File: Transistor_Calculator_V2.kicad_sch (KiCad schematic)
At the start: 50 parts, among them Q1 2N3904, Q10 2N3904, Q11 2N3904, Q12 2N3904, Q13 2N3904, Q14 2N3904, Q15 2N3904, Q16 2N3904, Q17 2N3904, Q18 2N3904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

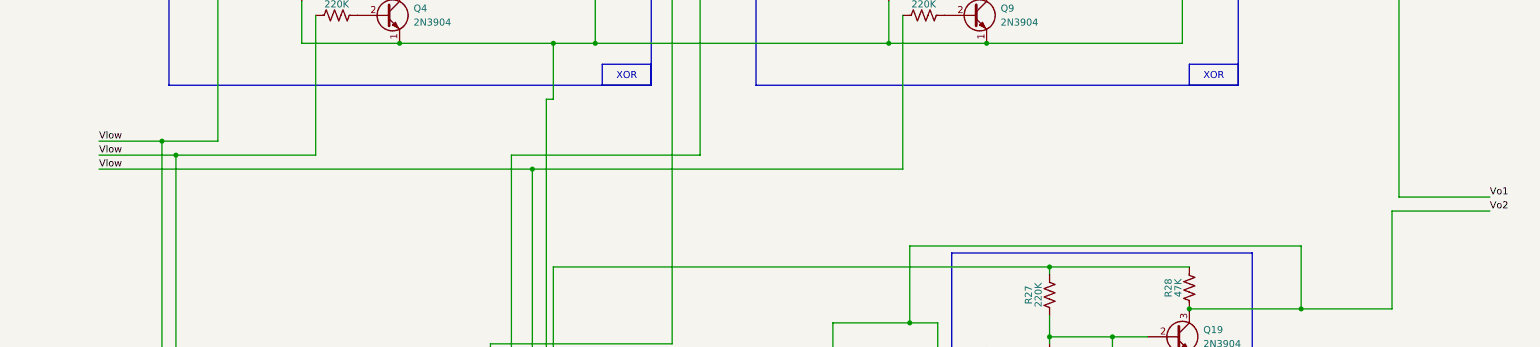
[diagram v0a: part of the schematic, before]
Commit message: added output labels
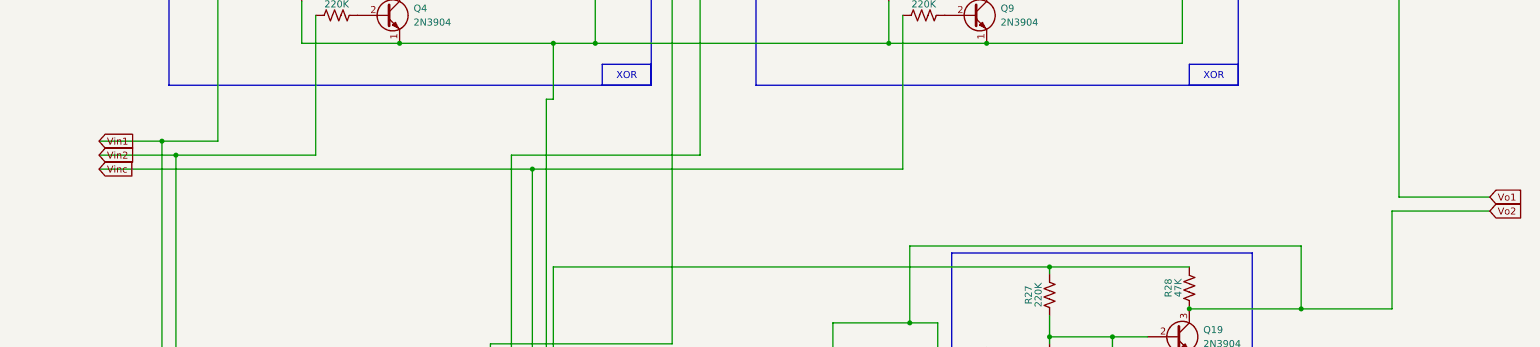
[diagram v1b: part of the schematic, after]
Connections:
- net Vlow: no longer R1.1, R10.1, R18.1, R19.1, R2.1, R21.1
- new net Vin1: R1.1, R18.1
- new net Vin2: R19.1, R2.1
- new net Vinc: R10.1, R21.1
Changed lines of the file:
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@@
-	)
-	(label "Vlow"
-		(at 17.78 105.41 0)
-		(fields_autoplaced yes)
-		(effects
-			(font
-				(size 1.27 1.27)
-			)
-			(justify left bottom)
-		)
-	)
-	(label "Vo1"
-		(at 270.51 113.03 0)
-		(fields_autoplaced yes)
-		(effects
-			(font
-				(size 1.27 1.27)
-			)
-			(justify left bottom)
-		)
 	)
 	(label "Vlow"
@@
 	(label "Vhigh"
 		(at -15.24 115.57 0)
-		(fields_autoplaced yes)
-		(effects
-			(font
-				(size 1.27 1.27)
-			)
-			(justify left bottom)
-		)
-	)
-	(label "Vlow"
-		(at 17.78 107.95 0)
-		(fields_autoplaced yes)
-		(effects
-			(font
-				(size 1.27 1.27)
-			)
-			(justify left bottom)
-		)
-	)
-	(label "Vo2"
-		(at 270.51 115.57 0)
-		(fields_autoplaced yes)
-		(effects
-			(font
-				(size 1.27 1.27)
-			)
-			(justify left bottom)
-		)
-	)
-	(label "Vlow"
-		(at 17.78 102.87 0)
 		(fields_autoplaced yes)
 		(effects
@@
 		)
 	)
+	(global_label "Vin1"
+		(shape input)
+		(at 17.78 102.87 0)
+		(fields_autoplaced yes)
+		(effects
+			(font
+				(size 1.27 1.27)
+			)
+			(justify left)
+		)
+		(property "Intersheetrefs" "${INTERSHEET_REFS}"
+			(at 24.8171 102.87 0)
+			(effects
+				(font
+					(size 1.27 1.27)
+				)
+				(justify left)
+				(hide yes)
+			)
+		)
+	)
+	(global_label "Vo1"
+		(shape input)
+		(at 270.51 113.03 0)
+		(fields_autoplaced yes)
+		(effects
+			(font
+				(size 1.27 1.27)
+			)
+			(justify left)
+		)
+		(property "Intersheetrefs" "${INTERSHEET_REFS}"
+			(at 276.9423 113.03 0)
+			(effects
+				(font
+					(size 1.27 1.27)
+				)
+				(justify left)
+				(hide yes)
+			)
+		)
+	)
+	(global_label "Vinc"
+		(shape input)
+		(at 17.78 107.95 0)
+		(fields_autoplaced yes)
+		(effects
+			(font
+				(size 1.27 1.27)
+			)
+			(justify left)
+		)
+		(property "Intersheetrefs" "${INTERSHEET_REFS}"
+			(at 24.6962 107.95 0)
+			(effects
+				(font
+					(size 1.27 1.27)
+				)
+				(justify left)
+				(hide yes)
+			)
+		)
+	)
+	(global_label "Vin2"
+		(shape input)
+		(at 17.78 105.41 0)
+		(fields_autoplaced yes)
+		(effects
+			(font
+				(size 1.27 1.27)
+			)
+			(justify left)
+		)
+		(property "Intersheetrefs" "${INTERSHEET_REFS}"
+			(at 24.8171 105.41 0)
+			(effects
+				(font
+					(size 1.27 1.27)
+				)
+				(justify left)
+				(hide yes)
+			)
+		)
+	)
+	(global_label "Vo2"
+		(shape input)
+		(at 270.51 115.57 0)
+		(fields_autoplaced yes)
+		(effects
+			(font
+				(size 1.27 1.27)
+			)
+			(justify left)
+		)
+		(property "Intersheetrefs" "${INTERSHEET_REFS}"
+			(at 276.9423 115.57 0)
+			(effects
+				(font
+					(size 1.27 1.27)
+				)
+				(justify left)
+				(hide yes)
+			)
+		)
+	)

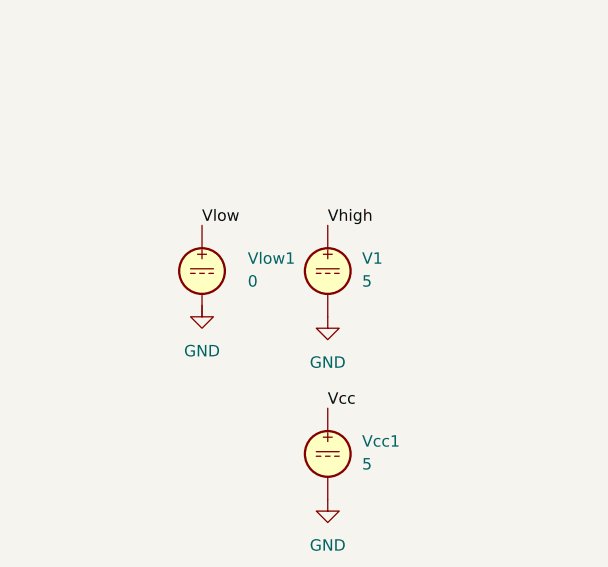
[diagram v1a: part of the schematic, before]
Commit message: Changed control of the input
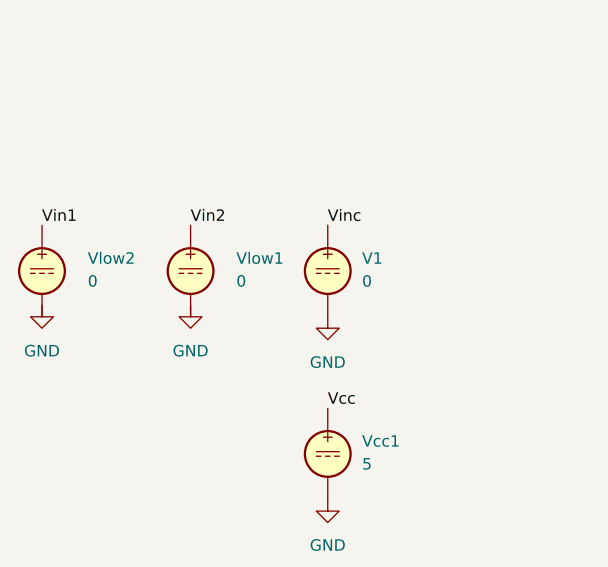
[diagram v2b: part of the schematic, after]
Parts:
- added Vlow2: 0, symbol Simulation_SPICE:VDC
- V1: value 5 -> 0
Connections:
- net Vhigh is gone; now on net Vinc: V1.1
- net Vlow is gone; now on net Vin2: Vlow1.1
- net Vin1: now also Vlow2.1
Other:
- moved on the sheet: Vlow1
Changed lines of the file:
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@@
 		)
 	)
-	(label "Vlow"
-		(at -29.21 115.57 0)
+	(label "Vin2"
+		(at -30.48 115.57 0)
 		(fields_autoplaced yes)
 		(effects
@@
 		)
 	)
-	(label "Vhigh"
+	(label "Vin1"
+		(at -46.99 115.57 0)
+		(fields_autoplaced yes)
+		(effects
+			(font
+				(size 1.27 1.27)
+			)
+			(justify left bottom)
+		)
+	)
+	(label "Vinc"
 		(at -15.24 115.57 0)
 		(fields_autoplaced yes)
@@
 	(symbol
 		(lib_id "power:GND")
-		(at -29.21 124.46 0)
+		(at -30.48 124.46 0)
 		(unit 1)
 		(exclude_from_sim no)
@@
 		(fields_autoplaced yes)
 		(property "Reference" "#PWR01"
-			(at -29.21 130.81 0)
+			(at -30.48 130.81 0)
 			(effects
 				(font
@@
 		)
 		(property "Value" "GND"
-			(at -29.21 129.54 0)
+			(at -30.48 129.54 0)
 			(effects
 				(font
@@
 		)
 		(property "Footprint" ""
-			(at -29.21 124.46 0)
+			(at -30.48 124.46 0)
 			(effects
 				(font
@@
 		)
 		(property "Datasheet" ""
-			(at -29.21 124.46 0)
+			(at -30.48 124.46 0)
 			(effects
 				(font
@@
 		)
 		(property "Description" "Power symbol creates a global label with name \"GND\" , ground"
-			(at -29.21 124.46 0)
+			(at -30.48 124.46 0)
 			(effects
 				(font
@@
 			)
 		)
-		(property "Value" "5"
+		(property "Value" "0"
 			(at -11.43 121.7901 0)
 			(effects
@@
 	(symbol
 		(lib_id "Simulation_SPICE:VDC")
-		(at -29.21 120.65 0)
+		(at -30.48 120.65 0)
 		(unit 1)
 		(exclude_from_sim no)
@@
 		(fields_autoplaced yes)
 		(property "Reference" "Vlow1"
-			(at -24.13 119.2501 0)
+			(at -25.4 119.2501 0)
 			(effects
 				(font
@@
 		)
 		(property "Value" "0"
-			(at -24.13 121.7901 0)
+			(at -25.4 121.7901 0)
 			(effects
 				(font
@@
 		)
 		(property "Footprint" ""
-			(at -29.21 120.65 0)
+			(at -30.48 120.65 0)
 			(effects
 				(font
@@
 		)
 		(property "Datasheet" "https://ngspice.sourceforge.io/docs/ngspice-html-manual/manual.xhtml#sec_Independent_Sources_for"
-			(at -29.21 120.65 0)
+			(at -30.48 120.65 0)
 			(effects
 				(font
@@
 		)
 		(property "Description" "Voltage source, DC"
-			(at -29.21 120.65 0)
+			(at -30.48 120.65 0)
 			(effects
 				(font
@@
 		)
 		(property "Sim.Pins" "1=+ 2=-"
-			(at -29.21 120.65 0)
+			(at -30.48 120.65 0)
 			(effects
 				(font
@@
 		)
 		(property "Sim.Type" "DC"
-			(at -29.21 120.65 0)
+			(at -30.48 120.65 0)
 			(effects
 				(font
@@
 		)
 		(property "Sim.Device" "V"
-			(at -29.21 120.65 0)
+			(at -30.48 120.65 0)
 			(effects
 				(font
@@
 	)
 	(symbol
+		(lib_id "power:GND")
+		(at -46.99 124.46 0)
+		(unit 1)
+		(exclude_from_sim no)
+		(in_bom yes)
+		(on_board yes)
+		(dnp no)
+		(fields_autoplaced yes)
+		(property "Reference" "#PWR05"
+			(at -46.99 130.81 0)
+			(effects
+				(font
+					(size 1.27 1.27)
+				)
+				(hide yes)
+			)
+		)
+		(property "Value" "GND"
+			(at -46.99 129.54 0)
+			(effects
+				(font
+					(size 1.27 1.27)
+				)
+			)
+		)
+		(property "Footprint" ""
+			(at -46.99 124.46 0)
+			(effects
+				(font
+					(size 1.27 1.27)
+				)
+				(hide yes)
+			)
+		)
+		(property "Datasheet" ""
+			(at -46.99 124.46 0)
+			(effects
+				(font
+					(size 1.27 1.27)
+				)
+				(hide yes)
+			)
+		)
+		(property "Description" "Power symbol creates a global label with name \"GND\" , ground"
+			(at -46.99 124.46 0)
+			(effects
+				(font
+					(size 1.27 1.27)
+				)
+				(hide yes)
+			)
+		)
+		(pin "1"
+		)
+		(instances
+			(project "Transistor_Calculator_V2"
+				(path "/4e74c2aa-3410-4407-95d8-73d62854742b"
+					(reference "#PWR05")
+					(unit 1)
+				)
+			)
+		)
+	)
+	(symbol
 		(lib_id "Transistor_BJT:2N3904")
 		(at 158.75 55.88 0)
@@
 					(unit 1)
 				)
+			)
+		)
+	)
+	(symbol
+		(lib_id "Simulation_SPICE:VDC")
+		(at -46.99 120.65 0)
+		(unit 1)
+		(exclude_from_sim no)
+		(in_bom yes)
+		(on_board yes)
+		(dnp no)
+		(fields_autoplaced yes)
+		(property "Reference" "Vlow2"
+			(at -41.91 119.2501 0)
+			(effects
+				(font
+					(size 1.27 1.27)
+				)
+				(justify left)
+			)
+		)
+		(property "Value" "0"
+			(at -41.91 121.7901 0)
+			(effects
+				(font
+					(size 1.27 1.27)
+				)
+				(justify left)
+			)
+		)
+		(property "Footprint" ""
+			(at -46.99 120.65 0)
+			(effects
+				(font
+					(size 1.27 1.27)
+				)
+				(hide yes)
+			)
+		)
+		(property "Datasheet" "https://ngspice.sourceforge.io/docs/ngspice-html-manual/manual.xhtml#sec_Independent_Sources_for"
+			(at -46.99 120.65 0)
+			(effects
+				(font
+					(size 1.27 1.27)
+				)
+				(hide yes)
+			)
+		)
+		(property "Description" "Voltage source, DC"
+			(at -46.99 120.65 0)
+			(effects
+				(font
+					(size 1.27 1.27)
+				)
+				(hide yes)
+			)
+		)
+		(property "Sim.Pins" "1=+ 2=-"
+			(at -46.99 120.65 0)
+			(effects
+				(font
+					(size 1.27 1.27)
+				)
+				(hide yes)
+			)
+		)
+		(property "Sim.Type" "DC"
+			(at -46.99 120.65 0)
+			(effects
+				(font
+					(size 1.27 1.27)
+				)
+				(hide yes)
+			)
+		)
+		(property "Sim.Device" "V"
+			(at -46.99 120.65 0)
+			(effects
+				(font
+					(size 1.27 1.27)
+				)
+				(justify left)
+				(hide yes)
+			)
+		)
+		(pin "1"
+		)
+		(pin "2"
+		)
+		(instances
+			(project "Transistor_Calculator_V2"
+				(path "/4e74c2aa-3410-4407-95d8-73d62854742b"
+					(reference "Vlow2")
+					(unit 1)
+				)

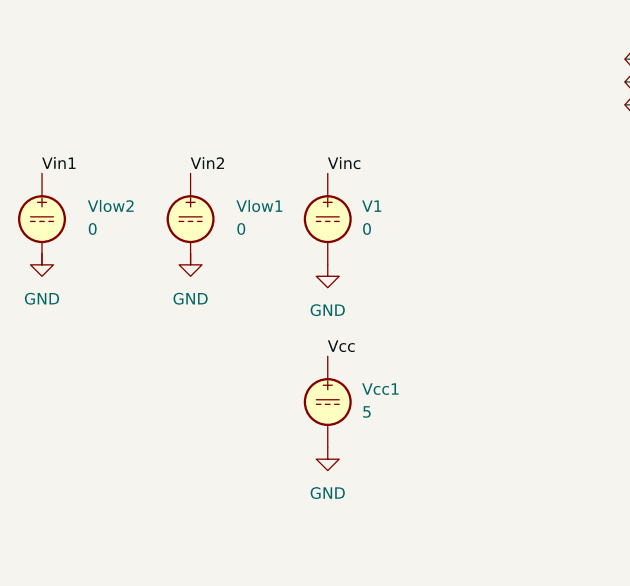
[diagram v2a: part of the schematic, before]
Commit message: Change voltage connectors
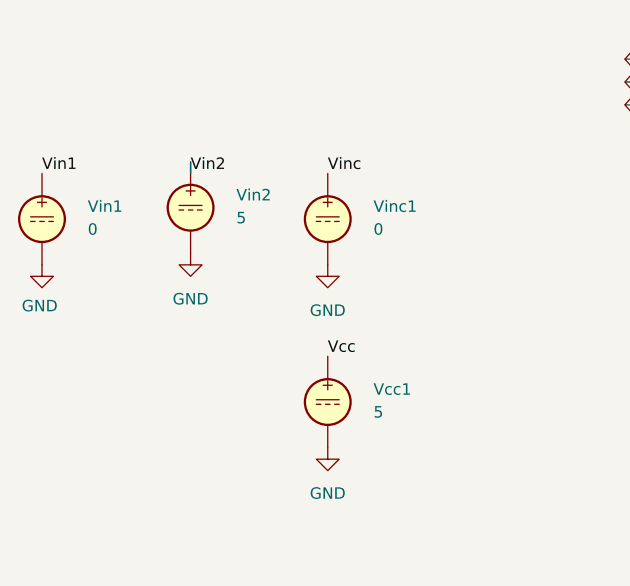
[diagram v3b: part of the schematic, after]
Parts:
- Vin2: renamed from Vlow1; value 0 -> 5
- renumbered Vlow2 to Vin1, V1 to Vinc1
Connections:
- net GND: now also Vin1.2, Vin2.2
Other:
- moved on the sheet: Vin2
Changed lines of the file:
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@@
 	(wire
 		(pts
+			(xy -30.48 114.3) (xy -30.48 115.57)
+		)
+		(stroke
+			(width 0)
+			(type default)
+		)
+	)
+	(wire
+		(pts
 			(xy 127 39.37) (xy 127 72.39)
 		)
@@
 		)
 	)
-	(global_label "Vin1"
+	(global_label "Vo1"
 		(shape input)
-		(at 17.78 102.87 0)
+		(at 270.51 113.03 0)
 		(fields_autoplaced yes)
 		(effects
@@
 		)
 		(property "Intersheetrefs" "${INTERSHEET_REFS}"
-			(at 24.8171 102.87 0)
+			(at 276.9423 113.03 0)
 			(effects
 				(font
@@
 		)
 	)
-	(global_label "Vo1"
+	(global_label "Vin2"
 		(shape input)
-		(at 270.51 113.03 0)
+		(at 17.78 105.41 0)
 		(fields_autoplaced yes)
 		(effects
@@
 		)
 		(property "Intersheetrefs" "${INTERSHEET_REFS}"
-			(at 276.9423 113.03 0)
+			(at 24.8171 105.41 0)
 			(effects
 				(font
@@
 		)
 	)
-	(global_label "Vinc"
+	(global_label "Vin1"
 		(shape input)
-		(at 17.78 107.95 0)
+		(at 17.78 102.87 0)
 		(fields_autoplaced yes)
 		(effects
@@
 		)
 		(property "Intersheetrefs" "${INTERSHEET_REFS}"
-			(at 24.6962 107.95 0)
+			(at 24.8171 102.87 0)
 			(effects
 				(font
@@
 		)
 	)
-	(global_label "Vin2"
+	(global_label "Vo2"
 		(shape input)
-		(at 17.78 105.41 0)
+		(at 270.51 115.57 0)
 		(fields_autoplaced yes)
 		(effects
@@
 		)
 		(property "Intersheetrefs" "${INTERSHEET_REFS}"
-			(at 24.8171 105.41 0)
+			(at 276.9423 115.57 0)
 			(effects
 				(font
@@
 		)
 	)
-	(global_label "Vo2"
+	(global_label "Vinc"
 		(shape input)
-		(at 270.51 115.57 0)
+		(at 17.78 107.95 0)
 		(fields_autoplaced yes)
 		(effects
@@
 		)
 		(property "Intersheetrefs" "${INTERSHEET_REFS}"
-			(at 276.9423 115.57 0)
+			(at 24.6962 107.95 0)
 			(effects
 				(font
@@
 		(fields_autoplaced yes)
 		(property "Reference" "Vcc1"
-			(at -11.43 139.5701 0)
+			(at -10.16 139.5701 0)
 			(effects
 				(font
@@
 		)
 		(property "Value" "5"
-			(at -11.43 142.1101 0)
+			(at -10.16 142.1101 0)
 			(effects
 				(font
@@
 		(dnp no)
 		(fields_autoplaced yes)
-		(property "Reference" "V1"
-			(at -11.43 119.2501 0)
+		(property "Reference" "Vinc1"
+			(at -10.16 119.2501 0)
 			(effects
 				(font
@@
 		)
 		(property "Value" "0"
-			(at -11.43 121.7901 0)
+			(at -10.16 121.7901 0)
 			(effects
 				(font
@@
 			(project "Transistor_Calculator_V2"
 				(path "/4e74c2aa-3410-4407-95d8-73d62854742b"
-					(reference "V1")
+					(reference "Vinc1")
 					(unit 1)
 				)
@@
 	(symbol
 		(lib_id "Simulation_SPICE:VDC")
-		(at -30.48 120.65 0)
+		(at -30.48 119.38 0)
 		(unit 1)
 		(exclude_from_sim no)
@@
 		(dnp no)
 		(fields_autoplaced yes)
-		(property "Reference" "Vlow1"
-			(at -25.4 119.2501 0)
+		(property "Reference" "Vin2"
+			(at -25.4 117.9801 0)
 			(effects
 				(font
@@
 			)
 		)
-		(property "Value" "0"
-			(at -25.4 121.7901 0)
+		(property "Value" "5"
+			(at -25.4 120.5201 0)
 			(effects
 				(font
@@
 		)
 		(property "Footprint" ""
-			(at -30.48 120.65 0)
+			(at -30.48 119.38 0)
 			(effects
 				(font
@@
 		)
 		(property "Datasheet" "https://ngspice.sourceforge.io/docs/ngspice-html-manual/manual.xhtml#sec_Independent_Sources_for"
-			(at -30.48 120.65 0)
+			(at -30.48 119.38 0)
 			(effects
 				(font
@@
 		)
 		(property "Description" "Voltage source, DC"
-			(at -30.48 120.65 0)
+			(at -30.48 119.38 0)
 			(effects
 				(font
@@
 		)
 		(property "Sim.Pins" "1=+ 2=-"
-			(at -30.48 120.65 0)
+			(at -30.48 119.38 0)
 			(effects
 				(font
@@
 		)
 		(property "Sim.Type" "DC"
-			(at -30.48 120.65 0)
+			(at -30.48 119.38 0)
 			(effects
 				(font
@@
 		)
 		(property "Sim.Device" "V"
-			(at -30.48 120.65 0)
+			(at -30.48 119.38 0)
 			(effects
 				(font
@@
 			(project "Transistor_Calculator_V2"
 				(path "/4e74c2aa-3410-4407-95d8-73d62854742b"
-					(reference "Vlow1")
+					(reference "Vin2")
 					(unit 1)
 				)
@@
 	(symbol
 		(lib_id "power:GND")
-		(at -46.99 124.46 0)
+		(at -46.99 125.73 0)
 		(unit 1)
 		(exclude_from_sim no)
@@
 		(on_board yes)
 		(dnp no)
-		(fields_autoplaced yes)
 		(property "Reference" "#PWR05"
-			(at -46.99 130.81 0)
+			(at -46.99 132.08 0)
 			(effects
 				(font
@@
 		)
 		(property "Value" "GND"
-			(at -46.99 129.54 0)
+			(at -47.244 130.302 0)
 			(effects
 				(font
@@
 		)
 		(property "Footprint" ""
-			(at -46.99 124.46 0)
+			(at -46.99 125.73 0)
 			(effects
 				(font
@@
 		)
 		(property "Datasheet" ""
-			(at -46.99 124.46 0)
+			(at -46.99 125.73 0)
 			(effects
 				(font
@@
 		)
 		(property "Description" "Power symbol creates a global label with name \"GND\" , ground"
-			(at -46.99 124.46 0)
+			(at -46.99 125.73 0)
 			(effects
 				(font
@@
 		(dnp no)
 		(fields_autoplaced yes)
-		(property "Reference" "Vlow2"
+		(property "Reference" "Vin1"
 			(at -41.91 119.2501 0)
 			(effects
@@
 			(project "Transistor_Calculator_V2"
 				(path "/4e74c2aa-3410-4407-95d8-73d62854742b"
-					(reference "Vlow2")
+					(reference "Vin1")
 					(unit 1)
 				)
